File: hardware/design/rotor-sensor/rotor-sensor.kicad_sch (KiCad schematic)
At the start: 93 parts, among them J2 Conn_01x06, J517 Conn_ARM_JTAG_SWD_10, U1 MCP2021A-500E/SN, U2 AP22804AW5, U5 AP22804AW5, U500 ATSAMD21E18A-A, U501 AP2127K-ADJTRG1, U600 BMI088, Y508 ABS07-32.768KHZ-7-T

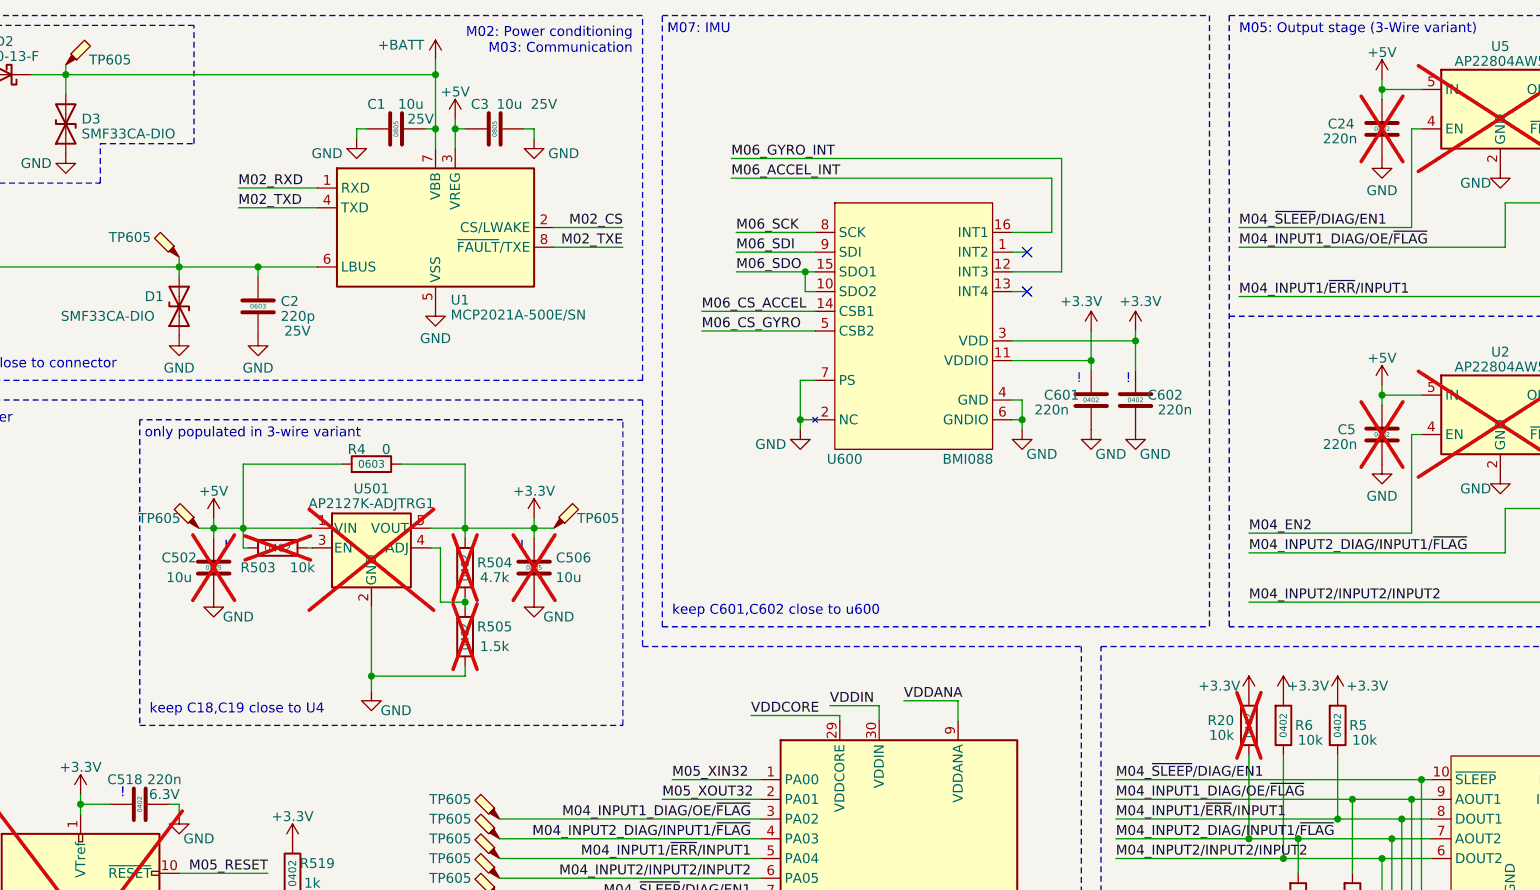
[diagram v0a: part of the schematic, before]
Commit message: Optical sensor adapter & CI workflow changes
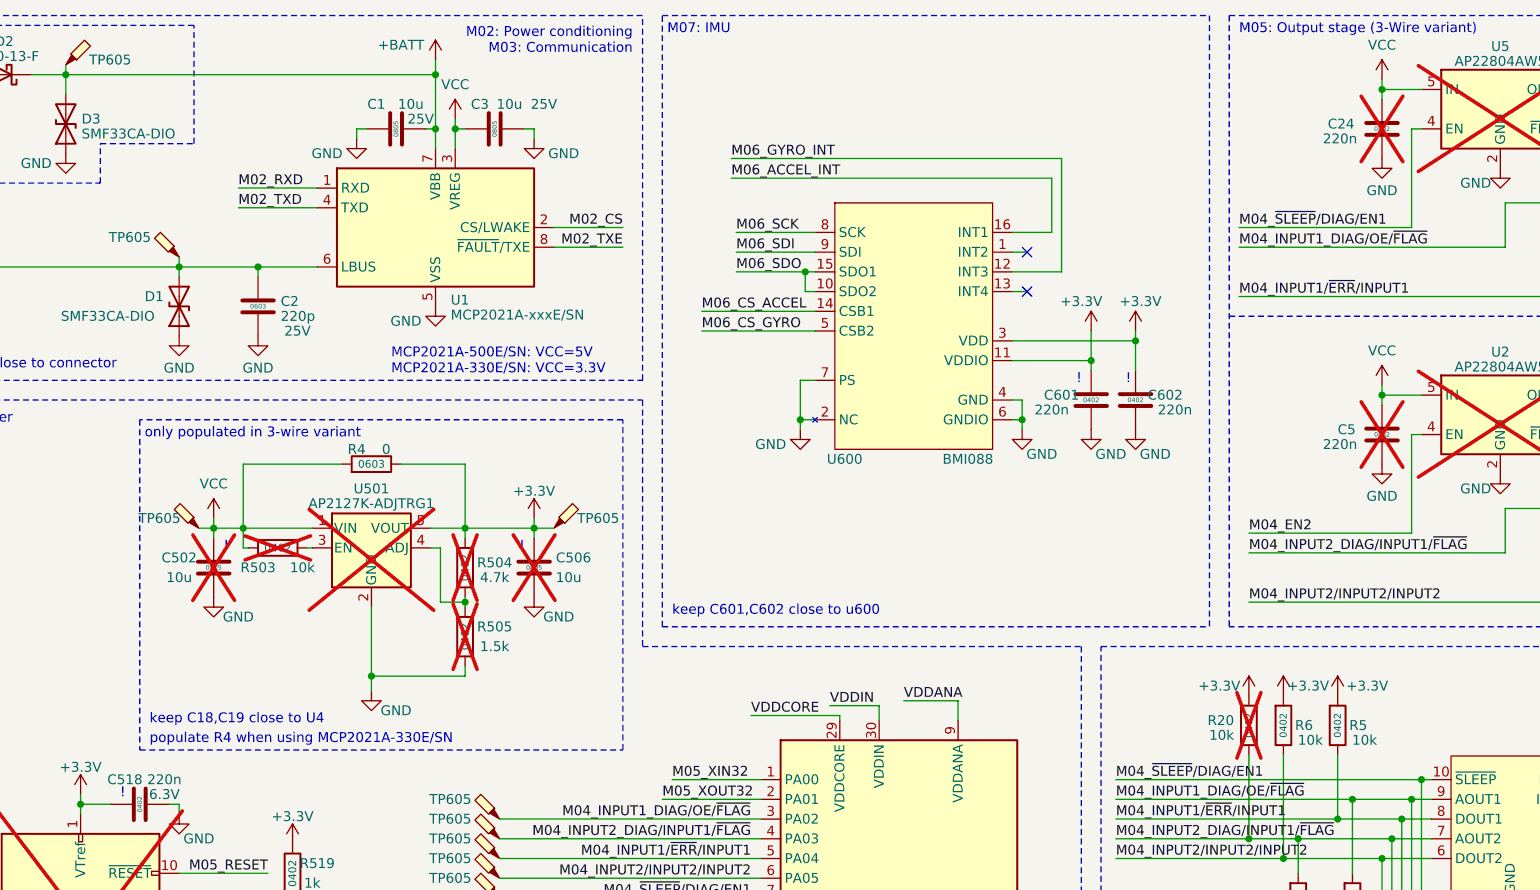
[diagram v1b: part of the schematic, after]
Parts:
- U1: value MCP2021A-500E/SN -> MCP2021A-xxxE/SN
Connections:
- net +5V: no longer C24.2, C3.1, C5.2, C502.2, R4.2, R503.1, TP605.1, U1.3 (VREG), U2.5 (IN), U5.5 (IN), U501.1 (VIN)
- new net VCC: C24.2, C3.1, C5.2, C502.2, R4.2, R503.1, TP605.1, U1.3 (VREG), U2.5 (IN), U5.5 (IN), U501.1 (VIN)
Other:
- note added: "MCP2021A-500E/SN: VCC=5V MCP2021A-330E/SN: VCC=3.3V"
- note added: "populate R4 when using MCP2021A-330E/SN"
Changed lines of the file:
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@@
     (stroke (width 0) (type default))
   )
-  (polyline (pts (xy 114.935 133.35) (xy 177.165 133.35))
+  (polyline (pts (xy 114.935 136.525) (xy 177.165 136.525))
     (stroke (width 0) (type dot))
   )
@@
     (stroke (width 0) (type default))
   )
-  (polyline (pts (xy 114.935 93.98) (xy 114.935 133.35))
+  (polyline (pts (xy 114.935 93.98) (xy 114.935 136.525))
     (stroke (width 0) (type dot))
   )
@@
     (stroke (width 0) (type default))
   )
-  (polyline (pts (xy 177.165 133.35) (xy 177.165 93.98))
+  (polyline (pts (xy 177.165 136.525) (xy 177.165 93.98))
     (stroke (width 0) (type dot))
   )
@@
     (effects (font (size 1.27 1.27)) (justify left bottom))
   )
+  (text "MCP2021A-500E/SN: VCC=5V\nMCP2021A-330E/SN: VCC=3.3V"
+    (at 147.32 88.265 0)
+    (effects (font (size 1.27 1.27)) (justify left bottom))
+  )
   (text "only populated in 3-wire variant" (at 115.57 96.52 0)
     (effects (font (size 1.27 1.27)) (justify left bottom))
   )
-  (text "keep C18,C19 close to U4" (at 116.205 132.08 0)
+  (text "keep C18,C19 close to U4" (at 116.205 133.35 0)
     (effects (font (size 1.27 1.27)) (justify left bottom))
   )
@@
     (effects (font (size 1.27 1.27)) (justify left bottom))
   )
+  (text "populate R4 when using MCP2021A-330E/SN" (at 116.205 135.89 0)
+    (effects (font (size 1.27 1.27)) (justify left bottom))
+  )
   (text "M06: Sensor Connector" (at 262.89 200.025 0)
     (effects (font (size 1.27 1.27)) (justify left bottom))
@@
     )
   )
+  (symbol (lib_id "power:VCC") (at 274.955 89.535 0) (unit 1)
+    (in_bom yes) (on_board yes) (dnp no) (fields_autoplaced)
+    (property "Reference" "#PWR021" (at 274.955 93.345 0)
+      (effects (font (size 1.27 1.27)) hide)
+    )
+    (property "Value" "VCC" (at 274.955 85.09 0)
+      (effects (font (size 1.27 1.27)))
+    )
+    (property "Footprint" "" (at 274.955 89.535 0)
+      (effects (font (size 1.27 1.27)) hide)
+    )
+    (property "Datasheet" "" (at 274.955 89.535 0)
+      (effects (font (size 1.27 1.27)) hide)
+    )
+    (pin "1")
+    (instances
+      (project "rotor-sensor"
+        (path "/d35462db-b405-4e6b-820c-984876fa429d"
+          (reference "#PWR021") (unit 1)
+        )
+      )
+    )
+  )
   (symbol (lib_id "Device:C") (at 336.55 142.875 0) (mirror x) (unit 1)
     (in_bom yes) (on_board yes) (dnp yes)
@@
     )
   )
-  (symbol (lib_id "power:+5V") (at 124.46 106.68 0) (unit 1)
-    (in_bom yes) (on_board yes) (dnp no) (fields_autoplaced)
-    (property "Reference" "#PWR021" (at 124.46 110.49 0)
-      (effects (font (size 1.27 1.27)) hide)
-    )
-    (property "Value" "+5V" (at 124.46 103.1781 0)
-      (effects (font (size 1.27 1.27)))
-    )
-    (property "Footprint" "" (at 124.46 106.68 0)
-      (effects (font (size 1.27 1.27)) hide)
-    )
-    (property "Datasheet" "" (at 124.46 106.68 0)
-      (effects (font (size 1.27 1.27)) hide)
-    )
-    (pin "1")
-    (instances
-      (project "rotor-sensor"
-        (path "/d35462db-b405-4e6b-820c-984876fa429d"
-          (reference "#PWR021") (unit 1)
-        )
-      )
-    )
-  )
   (symbol (lib_id "Device:C") (at 274.955 56.515 180) (unit 1)
     (in_bom yes) (on_board yes) (dnp yes)
@@
     )
   )
-  (symbol (lib_id "power:+5V") (at 274.955 89.535 0) (unit 1)
-    (in_bom yes) (on_board yes) (dnp no) (fields_autoplaced)
-    (property "Reference" "#PWR048" (at 274.955 93.345 0)
-      (effects (font (size 1.27 1.27)) hide)
-    )
-    (property "Value" "+5V" (at 274.955 86.0331 0)
-      (effects (font (size 1.27 1.27)))
-    )
-    (property "Footprint" "" (at 274.955 89.535 0)
-      (effects (font (size 1.27 1.27)) hide)
-    )
-    (property "Datasheet" "" (at 274.955 89.535 0)
-      (effects (font (size 1.27 1.27)) hide)
-    )
-    (pin "1")
-    (instances
-      (project "rotor-sensor"
-        (path "/d35462db-b405-4e6b-820c-984876fa429d"
-          (reference "#PWR048") (unit 1)
-        )
-      )
-    )
-  )
   (symbol (lib_id "power:GND") (at 109.855 227.33 0) (unit 1)
     (in_bom yes) (on_board yes) (dnp no)
@@
     )
   )
+  (symbol (lib_id "power:VCC") (at 155.575 55.245 0) (unit 1)
+    (in_bom yes) (on_board yes) (dnp no) (fields_autoplaced)
+    (property "Reference" "#PWR068" (at 155.575 59.055 0)
+      (effects (font (size 1.27 1.27)) hide)
+    )
+    (property "Value" "VCC" (at 155.575 50.8 0)
+      (effects (font (size 1.27 1.27)))
+    )
+    (property "Footprint" "" (at 155.575 55.245 0)
+      (effects (font (size 1.27 1.27)) hide)
+    )
+    (property "Datasheet" "" (at 155.575 55.245 0)
+      (effects (font (size 1.27 1.27)) hide)
+    )
+    (pin "1")
+    (instances
+      (project "rotor-sensor"
+        (path "/d35462db-b405-4e6b-820c-984876fa429d"
+          (reference "#PWR068") (unit 1)
+        )
+      )
+    )
+  )
   (symbol (lib_id "Connector:TestPoint_Probe") (at 161.29 153.035 90) (unit 1)
     (in_bom yes) (on_board yes) (dnp no)
@@
     )
   )
-  (symbol (lib_id "power:+5V") (at 155.575 55.245 0) (unit 1)
-    (in_bom yes) (on_board yes) (dnp no) (fields_autoplaced)
-    (property "Reference" "#PWR020" (at 155.575 59.055 0)
-      (effects (font (size 1.27 1.27)) hide)
-    )
-    (property "Value" "+5V" (at 155.575 51.7431 0)
-      (effects (font (size 1.27 1.27)))
-    )
-    (property "Footprint" "" (at 155.575 55.245 0)
-      (effects (font (size 1.27 1.27)) hide)
-    )
-    (property "Datasheet" "" (at 155.575 55.245 0)
-      (effects (font (size 1.27 1.27)) hide)
-    )
-    (pin "1")
-    (instances
-      (project "rotor-sensor"
-        (path "/d35462db-b405-4e6b-820c-984876fa429d"
-          (reference "#PWR020") (unit 1)
-        )
-      )
-    )
-  )
   (symbol (lib_id "Mechanical:Fiducial") (at 245.745 218.44 0) (unit 1)
     (in_bom yes) (on_board yes) (dnp no) (fields_autoplaced)
@@
     )
   )
-  (symbol (lib_id "power:+5V") (at 274.955 50.165 0) (unit 1)
+  (symbol (lib_id "power:VCC") (at 124.46 106.68 0) (unit 1)
     (in_bom yes) (on_board yes) (dnp no) (fields_autoplaced)
-    (property "Reference" "#PWR057" (at 274.955 53.975 0)
+    (property "Reference" "#PWR020" (at 124.46 110.49 0)
       (effects (font (size 1.27 1.27)) hide)
     )
-    (property "Value" "+5V" (at 274.955 46.6631 0)
+    (property "Value" "VCC" (at 124.46 102.235 0)
       (effects (font (size 1.27 1.27)))
     )
-    (property "Footprint" "" (at 274.955 50.165 0)
+    (property "Footprint" "" (at 124.46 106.68 0)
       (effects (font (size 1.27 1.27)) hide)
     )
-    (property "Datasheet" "" (at 274.955 50.165 0)
+    (property "Datasheet" "" (at 124.46 106.68 0)
       (effects (font (size 1.27 1.27)) hide)
     )
@@
       (project "rotor-sensor"
         (path "/d35462db-b405-4e6b-820c-984876fa429d"
-          (reference "#PWR057") (unit 1)
+          (reference "#PWR020") (unit 1)
         )
       )
@@
     )
   )
+  (symbol (lib_id "power:VCC") (at 274.955 50.165 0) (unit 1)
+    (in_bom yes) (on_board yes) (dnp no) (fields_autoplaced)
+    (property "Reference" "#PWR069" (at 274.955 53.975 0)
+      (effects (font (size 1.27 1.27)) hide)
+    )
+    (property "Value" "VCC" (at 274.955 45.72 0)
+      (effects (font (size 1.27 1.27)))
+    )
+    (property "Footprint" "" (at 274.955 50.165 0)
+      (effects (font (size 1.27 1.27)) hide)
+    )
+    (property "Datasheet" "" (at 274.955 50.165 0)
+      (effects (font (size 1.27 1.27)) hide)
+    )
+    (pin "1")
+    (instances
+      (project "rotor-sensor"
+        (path "/d35462db-b405-4e6b-820c-984876fa429d"
+          (reference "#PWR069") (unit 1)
+        )
+      )
+    )
+  )
   (symbol (lib_id "Device:C") (at 157.48 223.52 0) (mirror x) (unit 1)
     (in_bom yes) (on_board yes) (dnp no)
@@
       (effects (font (size 1.27 1.27)) (justify left))
     )
-    (property "Value" "MCP2021A-500E/SN" (at 154.9909 80.4785 0)
+    (property "Value" "MCP2021A-xxxE/SN" (at 154.9909 80.4785 0)
       (effects (font (size 1.27 1.27)) (justify left))
     )
@@
   )
   (symbol (lib_id "power:GND") (at 153.035 79.375 0) (unit 1)
-    (in_bom yes) (on_board yes) (dnp no) (fields_autoplaced)
+    (in_bom yes) (on_board yes) (dnp no)
     (property "Reference" "#PWR03" (at 153.035 85.725 0)
       (effects (font (size 1.27 1.27)) hide)
     )
-    (property "Value" "GND" (at 153.035 83.5105 0)
+    (property "Value" "GND" (at 149.225 81.28 0)
       (effects (font (size 1.27 1.27)))
     )
